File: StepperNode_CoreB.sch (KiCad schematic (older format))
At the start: 0 parts

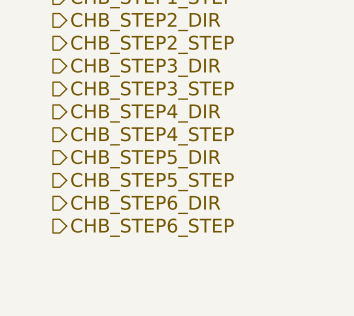
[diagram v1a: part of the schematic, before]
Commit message: Setup Watchdog Sheet
Watchdog is for Channel A/B priority determination.
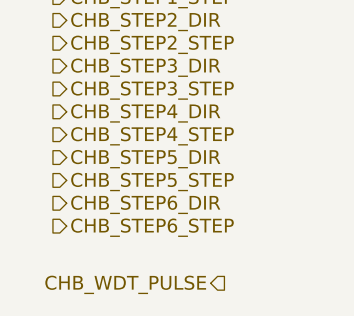
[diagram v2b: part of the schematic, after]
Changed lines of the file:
@@
 $Descr A3 16535 11693
 encoding utf-8
-Sheet 11 12
+Sheet 8 13
 Title ""
 Date ""
@@
 Text HLabel 1300 4050 2    60   Output ~ 0
 CHB_STEP6_STEP
+Text HLabel 2050 4300 0    60   Output ~ 0
+CHB_WDT_PULSE
 $EndSCHEMATC

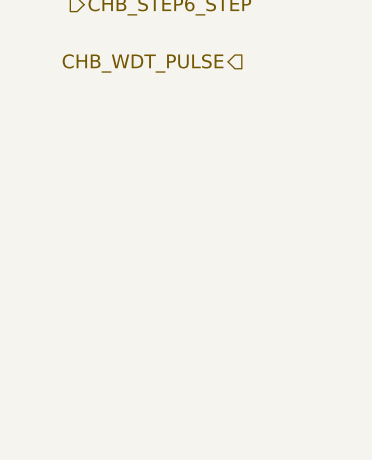
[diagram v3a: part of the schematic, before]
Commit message: Added Aux Prop Interface Sheet
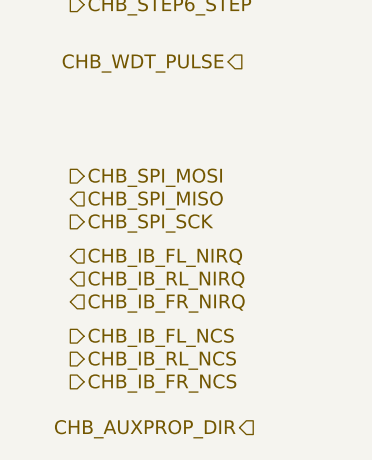
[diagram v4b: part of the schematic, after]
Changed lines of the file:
@@
 $Descr A3 16535 11693
 encoding utf-8
-Sheet 8 14
+Sheet 8 16
 Title ""
 Date ""
@@
 Text HLabel 2050 4300 0    60   Output ~ 0
 CHB_WDT_PULSE
+Text HLabel 1300 5150 2    60   Input ~ 0
+CHB_IB_FL_NIRQ
+Text HLabel 1300 5250 2    60   Input ~ 0
+CHB_IB_RL_NIRQ
+Text HLabel 1300 5350 2    60   Input ~ 0
+CHB_IB_FR_NIRQ
+Text HLabel 1300 5600 2    60   Output ~ 0
+CHB_IB_RL_NCS
+Text HLabel 1300 5700 2    60   Output ~ 0
+CHB_IB_FR_NCS
+Text HLabel 1300 5500 2    60   Output ~ 0
+CHB_IB_FL_NCS
+Text HLabel 1300 4800 2    60   Output ~ 0
+CHB_SPI_MOSI
+Text HLabel 1300 4900 2    60   Input ~ 0
+CHB_SPI_MISO
+Text HLabel 1300 5000 2    60   Output ~ 0
+CHB_SPI_SCK
+Text HLabel 2100 5900 0    60   Output ~ 0
+CHB_AUXPROP_DIR
 $EndSCHEMATC

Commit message: Netlist top level
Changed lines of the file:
@@
 $Descr A3 16535 11693
 encoding utf-8
-Sheet 8 16
+Sheet 7 16
 Title ""
 Date ""
@@
 Text HLabel 2100 5900 0    60   Output ~ 0
 CHB_AUXPROP_DIR
+Text HLabel 1950 6150 0    60   Input ~ 0
+PUSH_INTLK_A
+Text HLabel 1950 6250 0    60   Input ~ 0
+PUSH_INTLK_B
+Text HLabel 1250 6550 2    60   Input ~ 0
+CHB_ACCEL1_NINT
+Text HLabel 1250 6650 2    60   Input ~ 0
+CHB_ACCEL2_NINT
 $EndSCHEMATC

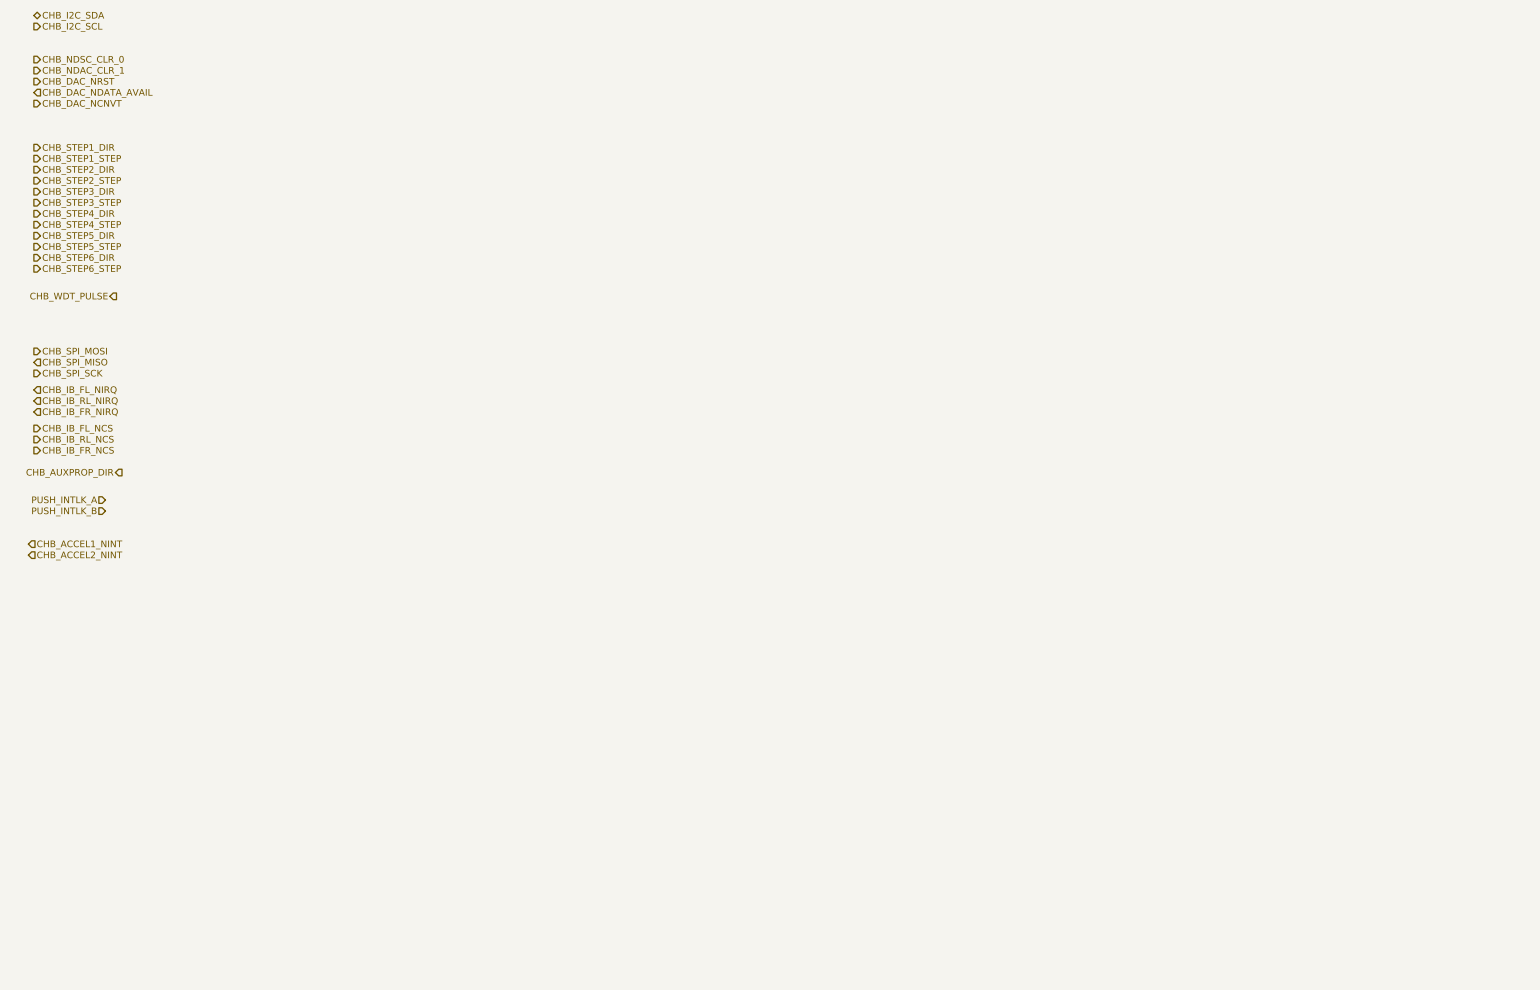
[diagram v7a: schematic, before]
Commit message: Updated node core connector pages and added interlocks.
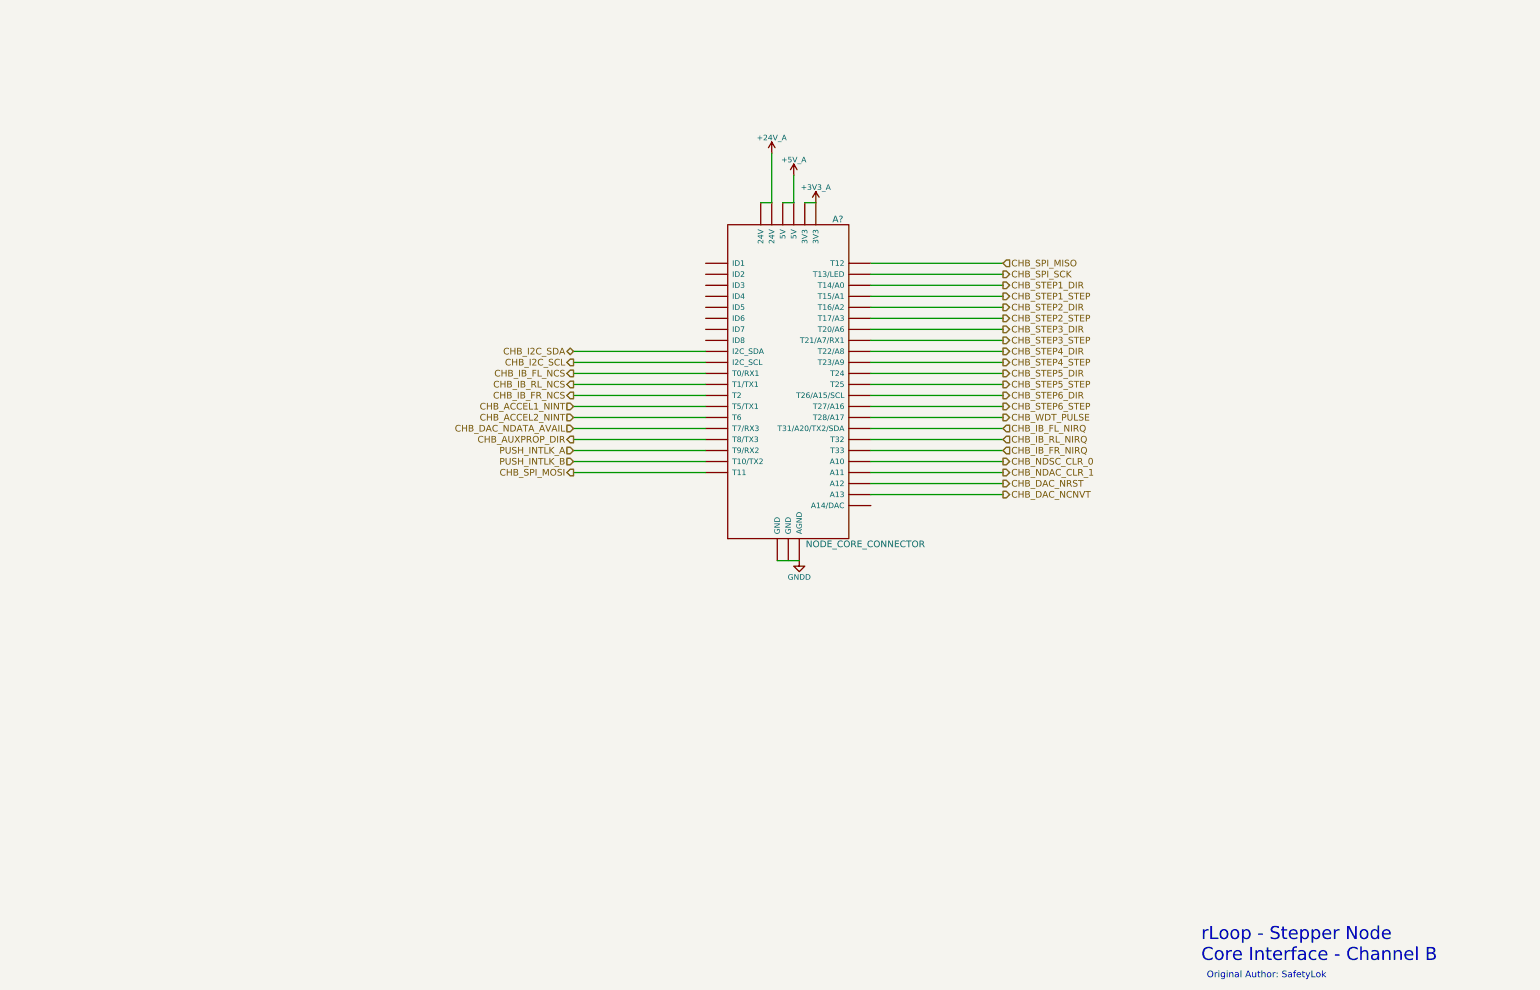
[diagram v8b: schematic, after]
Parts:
- added A?: NODE_CORE_CONNECTOR, symbol NODE_CORE_CONNECTOR-RESCUE-rloopStepperNode
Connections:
- net CHB_ACCEL1_NINT: now also A?.T5 (T5/TX1)
- net CHB_ACCEL2_NINT: now also A?.T6
- net CHB_AUXPROP_DIR: now also A?.T8 (T8/TX3)
- net CHB_DAC_NCNVT: now also A?.A13
- net CHB_DAC_NDATA_AVAIL: now also A?.T7 (T7/RX3)
- net CHB_DAC_NRST: now also A?.A12
- net CHB_I2C_SCL: now also A?.~ (ID8)
- net CHB_I2C_SDA: now also A?.~ (ID8)
- net CHB_IB_FL_NCS: now also A?.T0 (T0/RX1)
- net CHB_IB_FL_NIRQ: now also A?.T31 (T31/A20/TX2/SDA)
- net CHB_IB_FR_NCS: now also A?.T2
- net CHB_IB_FR_NIRQ: now also A?.T33
- net CHB_IB_RL_NCS: now also A?.T1 (T1/TX1)
- net CHB_IB_RL_NIRQ: now also A?.T32
- net CHB_NDAC_CLR_1: now also A?.A11
- net CHB_NDSC_CLR_0: now also A?.A10
- net CHB_SPI_MISO: now also A?.T12
- net CHB_SPI_MOSI: now also A?.T11
- net CHB_SPI_SCK: now also A?.T13 (T13/LED)
- net CHB_STEP1_DIR: now also A?.T14 (T14/A0)
- net CHB_STEP1_STEP: now also A?.T15 (T15/A1)
- net CHB_STEP2_DIR: now also A?.T16 (T16/A2)
- net CHB_STEP2_STEP: now also A?.T17 (T17/A3)
- net CHB_STEP3_DIR: now also A?.T20 (T20/A6)
- net CHB_STEP3_STEP: now also A?.T21 (T21/A7/RX1)
- net CHB_STEP4_DIR: now also A?.T22 (T22/A8)
- net CHB_STEP4_STEP: now also A?.T23 (T23/A9)
- net CHB_STEP5_DIR: now also A?.T24
- net CHB_STEP5_STEP: now also A?.T25
- net CHB_STEP6_DIR: now also A?.T26 (T26/A15/SCL)
- net CHB_STEP6_STEP: now also A?.T27 (T27/A16)
- net CHB_WDT_PULSE: now also A?.T28 (T28/A17)
- net PUSH_INTLK_A: now also A?.T9 (T9/RX2)
- net PUSH_INTLK_B: now also A?.T10 (T10/TX2)
- new net +3V3: A?.+3V3 (3V3)
- new net +5V: A?.+24V (24V), A?.+5V (5V)
- new net GNDD: A?.AGND, A?.GND
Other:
- note added: "Original Author: SafetyLok"
- note added: "rLoop - Stepper Node\nCore Interface - Channel B\n"
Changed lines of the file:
@@
 encoding utf-8
 Sheet 7 17
-Title ""
+Title "Core Interface - Channel B"
 Date ""
 Rev "1"
@@
 Comment4 ""
 $EndDescr
-Text HLabel 1300 1750 2    60   BiDi ~ 0
+$Comp
+L NODE_CORE_CONNECTOR-RESCUE-rloopStepperNode A?
+U 1 1 575E045E
+P 8150 5000
+F 0 "A?" H 8600 6400 60  0000 C CNN
+F 1 "NODE_CORE_CONNECTOR" H 8850 3450 60  0000 C CNN
+F 2 "" H 8150 5000 60  0000 C CNN
+F 3 "" H 8150 5000 60  0000 C CNN
+	1    8150 5000
+	1    0    0    -1
+$EndComp
+Text HLabel 10100 5800 2    60   Output ~ 0
+CHB_NDSC_CLR_0
+Text HLabel 10100 5900 2    60   Output ~ 0
+CHB_NDAC_CLR_1
+Text HLabel 10100 6000 2    60   Output ~ 0
+CHB_DAC_NRST
+Text HLabel 6200 5500 0    60   Input ~ 0
+CHB_DAC_NDATA_AVAIL
+Text HLabel 10100 6100 2    60   Output ~ 0
+CHB_DAC_NCNVT
+Text HLabel 10100 4200 2    60   Output ~ 0
+CHB_STEP1_DIR
+Text HLabel 10100 4300 2    60   Output ~ 0
+CHB_STEP1_STEP
+Text HLabel 10100 4400 2    60   Output ~ 0
+CHB_STEP2_DIR
+Text HLabel 10100 4500 2    60   Output ~ 0
+CHB_STEP2_STEP
+Text HLabel 10100 4600 2    60   Output ~ 0
+CHB_STEP3_DIR
+Text HLabel 10100 4700 2    60   Output ~ 0
+CHB_STEP3_STEP
+Text HLabel 10100 4800 2    60   Output ~ 0
+CHB_STEP4_DIR
+Text HLabel 10100 4900 2    60   Output ~ 0
+CHB_STEP4_STEP
+Text HLabel 10100 5000 2    60   Output ~ 0
+CHB_STEP5_DIR
+Text HLabel 10100 5100 2    60   Output ~ 0
+CHB_STEP5_STEP
+Text HLabel 10100 5200 2    60   Output ~ 0
+CHB_STEP6_DIR
+Text HLabel 10100 5300 2    60   Output ~ 0
+CHB_STEP6_STEP
+Text HLabel 10100 5400 2    60   Output ~ 0
+CHB_WDT_PULSE
+Text HLabel 10100 5500 2    60   Input ~ 0
+CHB_IB_FL_NIRQ
+Text HLabel 10100 5600 2    60   Input ~ 0
+CHB_IB_RL_NIRQ
+Text HLabel 10100 5700 2    60   Input ~ 0
+CHB_IB_FR_NIRQ
+Text HLabel 6200 5100 0    60   Output ~ 0
+CHB_IB_RL_NCS
+Text HLabel 6200 5200 0    60   Output ~ 0
+CHB_IB_FR_NCS
+Text HLabel 6200 5000 0    60   Output ~ 0
+CHB_IB_FL_NCS
+Text HLabel 6200 5900 0    60   Output ~ 0
+CHB_SPI_MOSI
+Text HLabel 6200 5600 0    60   Output ~ 0
+CHB_AUXPROP_DIR
+Text HLabel 6200 5700 0    60   Input ~ 0
+PUSH_INTLK_A
+Text HLabel 6200 5800 0    60   Input ~ 0
+PUSH_INTLK_B
+Text HLabel 6200 5300 0    60   Input ~ 0
+CHB_ACCEL1_NINT
+Text HLabel 6200 5400 0    60   Input ~ 0
+CHB_ACCEL2_NINT
+$Comp
+L +3V3_A #PWR?
+U 1 1 575E0483
+P 8400 3450
+F 0 "#PWR?" H 8400 3300 50  0001 C CNN
+F 1 "+3V3_A" H 8400 3590 50  0000 C CNN
+F 2 "" H 8400 3450 60  0000 C CNN
+F 3 "" H 8400 3450 60  0000 C CNN
+	1    8400 3450
+	1    0    0    -1
+$EndComp
+$Comp
+L +5V_A #PWR?
+U 1 1 575E0489
+P 8200 3200
+F 0 "#PWR?" H 8200 3050 50  0001 C CNN
+F 1 "+5V_A" H 8200 3340 50  0000 C CNN
+F 2 "" H 8200 3200 60  0000 C CNN
+F 3 "" H 8200 3200 60  0000 C CNN
+	1    8200 3200
+	1    0    0    -1
+$EndComp
+$Comp
+L +24V_A #PWR?
+U 1 1 575E048F
+P 8000 3000
+F 0 "#PWR?" H 8000 2850 50  0001 C CNN
+F 1 "+24V_A" H 8000 3140 50  0000 C CNN
+F 2 "" H 8000 3000 60  0000 C CNN
+F 3 "" H 8000 3000 60  0000 C CNN
+	1    8000 3000
+	1    0    0    -1
+$EndComp
+Wire Wire Line
+	8000 3000 8000 3450
+Wire Wire Line
+	8000 3450 7900 3450
+Wire Wire Line
+	8200 3200 8200 3450
+Wire Wire Line
+	8200 3450 8100 3450
+Wire Wire Line
+	8300 3450 8400 3450
+$Comp
+L GNDD #PWR?
+U 1 1 575E049A
+P 8250 6700
+F 0 "#PWR?" H 8250 6450 50  0001 C CNN
+F 1 "GNDD" H 8250 6550 50  0000 C CNN
+F 2 "" H 8250 6700 50  0000 C CNN
+F 3 "" H 8250 6700 50  0000 C CNN
+	1    8250 6700
+	1    0    0    -1
+$EndComp
+Wire Wire Line
+	8050 6700 8250 6700
+Wire Wire Line
+	7400 4800 6200 4800
+Wire Wire Line
+	7400 4900 6200 4900
+Text HLabel 6200 4800 0    60   BiDi ~ 0
 CHB_I2C_SDA
-Text HLabel 1300 1850 2    60   Output ~ 0
+Text HLabel 6200 4900 0    60   Output ~ 0
 CHB_I2C_SCL
-Text HLabel 1300 2150 2    60   Output ~ 0
-CHB_NDSC_CLR_0
-Text HLabel 1300 2250 2    60   Output ~ 0
-CHB_NDAC_CLR_1
-Text HLabel 1300 2350 2    60   Output ~ 0
-CHB_DAC_NRST
-Text HLabel 1300 2450 2    60   Input ~ 0
-CHB_DAC_NDATA_AVAIL
-Text HLabel 1300 2550 2    60   Output ~ 0
-CHB_DAC_NCNVT
-Text HLabel 1300 2950 2    60   Output ~ 0
-CHB_STEP1_DIR
-Text HLabel 1300 3050 2    60   Output ~ 0
-CHB_STEP1_STEP
-Text HLabel 1300 3150 2    60   Output ~ 0
-CHB_STEP2_DIR
-Text HLabel 1300 3250 2    60   Output ~ 0
-CHB_STEP2_STEP
-Text HLabel 1300 3350 2    60   Output ~ 0
-CHB_STEP3_DIR
-Text HLabel 1300 3450 2    60   Output ~ 0
-CHB_STEP3_STEP
-Text HLabel 1300 3550 2    60   Output ~ 0
-CHB_STEP4_DIR
-Text HLabel 1300 3650 2    60   Output ~ 0
-CHB_STEP4_STEP
-Text HLabel 1300 3750 2    60   Output ~ 0
-CHB_STEP5_DIR
-Text HLabel 1300 3850 2    60   Output ~ 0
-CHB_STEP5_STEP
-Text HLabel 1300 3950 2    60   Output ~ 0
-CHB_STEP6_DIR
-Text HLabel 1300 4050 2    60   Output ~ 0
-CHB_STEP6_STEP
-Text HLabel 2050 4300 0    60   Output ~ 0
-CHB_WDT_PULSE
-Text HLabel 1300 5150 2    60   Input ~ 0
-CHB_IB_FL_NIRQ
-Text HLabel 1300 5250 2    60   Input ~ 0
-CHB_IB_RL_NIRQ
-Text HLabel 1300 5350 2    60   Input ~ 0
-CHB_IB_FR_NIRQ
-Text HLabel 1300 5600 2    60   Output ~ 0
-CHB_IB_RL_NCS
-Text HLabel 1300 5700 2    60   Output ~ 0
-CHB_IB_FR_NCS
-Text HLabel 1300 5500 2    60   Output ~ 0
-CHB_IB_FL_NCS
-Text HLabel 1300 4800 2    60   Output ~ 0
-CHB_SPI_MOSI
-Text HLabel 1300 4900 2    60   Input ~ 0
+Wire Wire Line
+	7400 5000 6200 5000
+Wire Wire Line
+	7400 5100 6200 5100
+Wire Wire Line
+	7400 5200 6200 5200
+Wire Wire Line
+	7400 5900 6200 5900
+Wire Wire Line
+	10100 4000 8900 4000
+Wire Wire Line
+	10100 4100 8900 4100
+Text HLabel 10100 4000 2    60   Input ~ 0
 CHB_SPI_MISO
-Text HLabel 1300 5000 2    60   Output ~ 0
+Text HLabel 10100 4100 2    60   Output ~ 0
 CHB_SPI_SCK
-Text HLabel 2100 5900 0    60   Output ~ 0
-CHB_AUXPROP_DIR
-Text HLabel 1950 6150 0    60   Input ~ 0
-PUSH_INTLK_A
-Text HLabel 1950 6250 0    60   Input ~ 0
-PUSH_INTLK_B
-Text HLabel 1250 6550 2    60   Input ~ 0
-CHB_ACCEL1_NINT
-Text HLabel 1250 6650 2    60   Input ~ 0
-CHB_ACCEL2_NINT
+Wire Wire Line
+	10100 4200 8900 4200
+Wire Wire Line
+	10100 4300 8900 4300
+Wire Wire Line
+	10100 4400 8900 4400
+Wire Wire Line
+	10100 4500 8900 4500
+Wire Wire Line
+	10100 4600 8900 4600
+Wire Wire Line
+	10100 4700 8900 4700
+Wire Wire Line
+	10100 4800 8900 4800
+Wire Wire Line
+	10100 4900 8900 4900
+Wire Wire Line
+	10100 5000 8900 5000
+Wire Wire Line
+	10100 5500 8900 5500
+Wire Wire Line
+	10100 5600 8900 5600
+Wire Wire Line
+	10100 5700 8900 5700
+Wire Wire Line
+	10100 5100 8900 5100
+Wire Wire Line
+	10100 5200 8900 5200
+Wire Wire Line
+	10100 5300 8900 5300
+Wire Wire Line
+	10100 5400 8900 5400
+Wire Wire Line
+	10100 5900 8900 5900
+Wire Wire Line
+	10100 6000 8900 6000
+Wire Wire Line
+	10100 6100 8900 6100
+Wire Wire Line
+	10100 5800 8900 5800
+Wire Wire Line
+	7400 5300 6200 5300
+Wire Wire Line
+	7400 5400 6200 5400
+Wire Wire Line
+	7400 5500 6200 5500
+Wire Wire Line
+	7400 5600 6200 5600
+Wire Wire Line
+	7400 5700 6200 5700
+Wire Wire Line
+	7400 5800 6200 5800
+Text Notes 11900 10350 0    118  ~ 0
+rLoop - Stepper Node\nCore Interface - Channel B\n
+Text Notes 11950 10500 0    60   ~ 0
+Original Author: SafetyLok
 $EndSCHEMATC
